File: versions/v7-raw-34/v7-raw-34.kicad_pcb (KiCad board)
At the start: 4 copper layers, 138.1 x 104.6 mm, 133 parts, among them J1 USB_C_Receptacle_USB2.0, J10 AXT-310124, J11 THD2528-11SD-GF, J12 SM04B-SRSS-TB_LF__SN_, J2 EXTENSION_HEADER, J3 USB_HDR, J4 Conn_01x08_Pin, J5 CONN_BAT, J6 FH34SRJ-6S-0.5SH_99_, J7 ESP_HDR, J8 ESP_XTR_HDR, J9 Conn_01x08_Pin, Q1 AO3401A, Q3 MMBT3904, Q4 MMBT3904, U1 RT9080-33GJ5, U10 ED060XC5, U11 TP4056, U12 RY3730, U2 PCA9535PW, U3 RSL48_4P4X4P4, U4 USBLC6-2P6, U5 XC6206PxxxMR, U6 RY3730, U8 ESP32-S3-WROOM-1, U9 CH340C

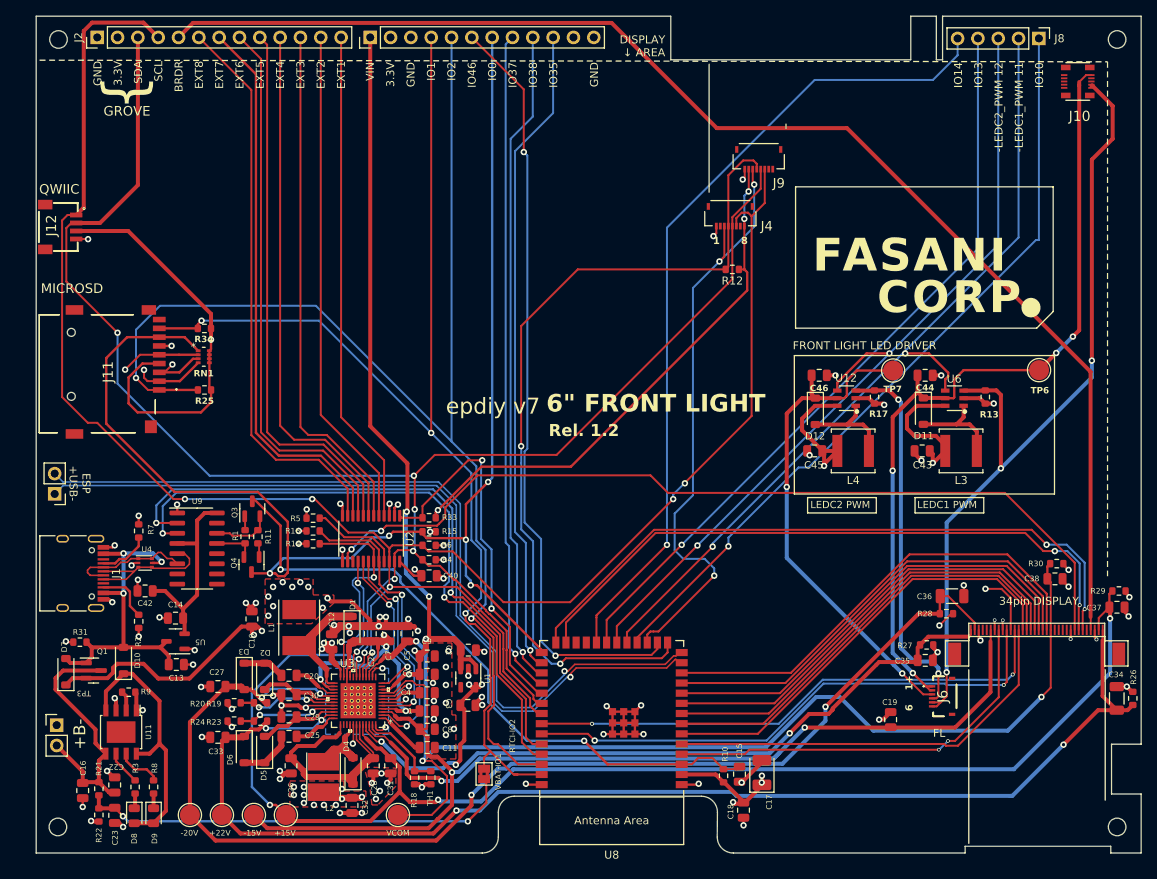
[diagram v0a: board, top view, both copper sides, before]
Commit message: Add kindle 34 pins versions (RAW)
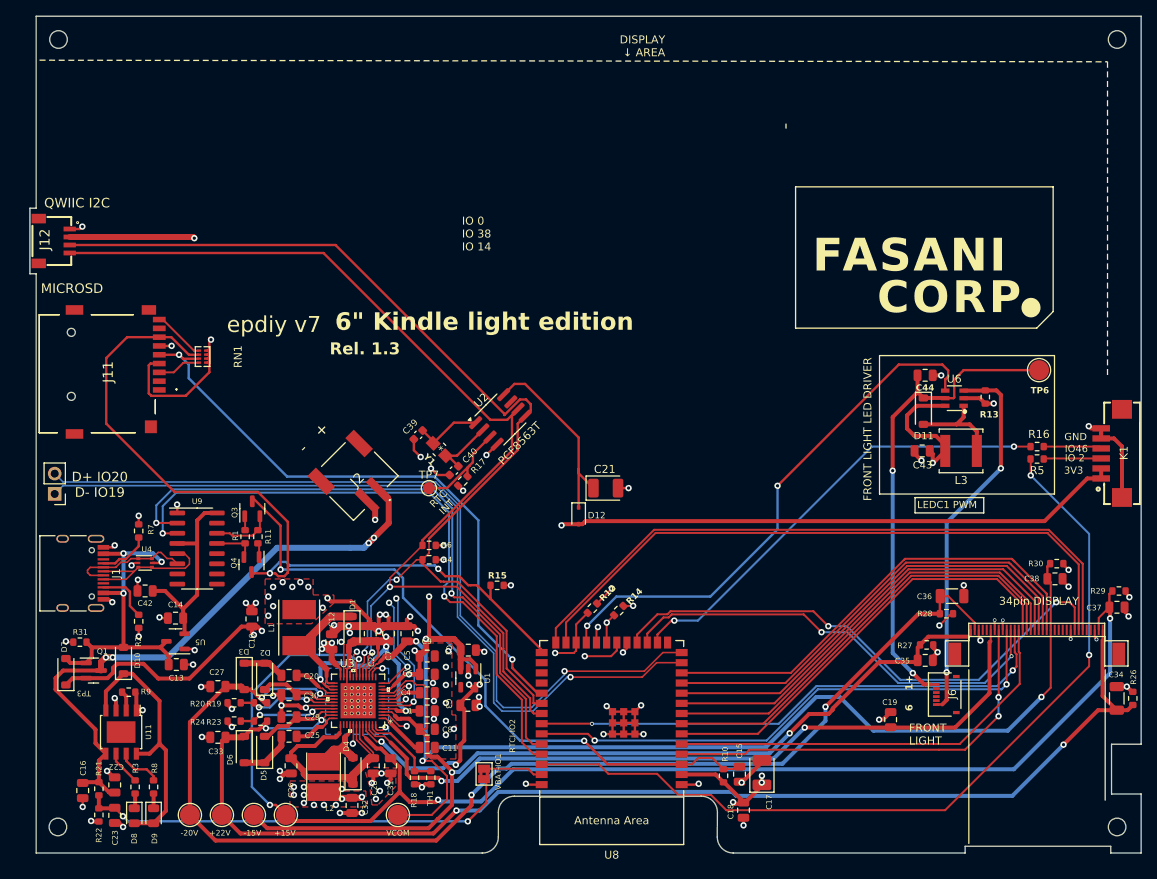
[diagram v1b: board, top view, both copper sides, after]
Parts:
- removed C45: 10uF, Capacitor_SMD:C_0805_2012Metric
- removed C46: 1uF/25V, Capacitor_SMD:C_0805_2012Metric
- removed J10: AXT-310124, footprint:AXT310124
- removed J4, J9: Conn_01x08_Pin, footprint:CONN8_FH34SRJ_HIR
- removed J5: CONN_BAT, Connector_PinHeader_2.54mm:PinHeader_1x02_P2.54mm_Vertical
- removed J7: ESP_HDR, Connector_PinHeader_2.54mm:PinHeader_1x12_P2.54mm_Vertical
- removed J8: ESP_XTR_HDR, Connector_PinHeader_2.54mm:PinHeader_1x05_P2.54mm_Vertical
- removed L4: L, footprint:SWPA5040S282MT
- removed R25, R34: 33k, Resistor_SMD:R_0603_1608Metric
- removed R33: 10k, Resistor_SMD:R_0603_1608Metric
- removed REF**: OSHW-Logo2_9.8x8mm_SilkScreen, Symbol:OSHW-Logo2_9.8x8mm_SilkScreen
- removed U12: RY3730, footprint:SOT-23-6_RY3730_Led_PWM
- added C21: C_Polarized 100uF, Capacitor_Tantalum_SMD:CP_EIA-3528-21_Kemet-B, F.Cu at (131.1, 103.0)
- added C39: 12 pF, Capacitor_SMD:C_0603_1608Metric, F.Cu at (107.6, 96.3)
- added K1: HC-1.25-6PWT, footprint:CONN-SMD_6P-P1.25_HC-1.25-6PWT, F.Cu at (194.3, 98.7)
- added Y1: Crystal_Small, footprint:Q13FC1350000400-Crystal, F.Cu at (110.3, 98.2)
- C40: value 100nF -> 12 pF; footprint Capacitor_SMD:C_0805_2012Metric -> Capacitor_SMD:C_0603_1608Metric
- D12: value MBR0540 -> 1N4148WS; footprint Diode_SMD:D_SOD-123 -> Diode_SMD:D_SOD-323
- J2: value EXTENSION_HEADER -> S2B-PH-SM4-TB_LF__SN_; footprint Connector_PinHeader_2.54mm:PinHeader_1x13_P2.54mm_Vertical -> footprint:S2BPHSM4TBLFSN
- J6: footprint footprint:FH34SRJ6S05SH99_Mirrored -> footprint:C224194_6x1_FH34SRJ-6S-0.5SH50_HIR
- L3: value L -> 22 uH
- R16: value 10k -> 0R
- R17: value 25Ω -> 10 K
- R3, R8: value 1k -> 2.4k
- R5: value 0 -> 0R
- R9: value 6.8k -> 3.8k
- RN1: footprint footprint:RESN_F392JTCE_UNR_SD-pullup -> footprint:C425297_RES-ARRAY-SMD_0402-8P-L2.0-W1.0-BL
- TP7: value C2 -> RTC_INT; footprint TestPoint:TestPoint_Pad_D2.5mm -> TestPoint:TestPoint_Pad_D1.5mm
- U2: value PCA9535PW -> PCF8563T; footprint Package_SO:TSSOP-24_4.4x7.8mm_P0.65mm -> Package_SO:SOIC-8_3.9x4.9mm_P1.27mm
- U3: value RSL48_4P4X4P4 -> TPS651851RSLR
- moved R16 91.1 mm to (185.0, 97.8), turned to 180 degrees
- moved R5 90.8 mm to (185.0, 99.3)
- moved J2 63.6 mm to (99.7, 101.5), turned to 45 degrees
- moved TP7 59.9 mm to (109.0, 103.0)
- moved R17 52.5 mm to (113.2, 102.1), turned to 45 degrees
- moved R12 45.8 mm to (129.4, 118.0), turned to -135 degrees
- moved R14 39.1 mm to (132.7, 118.3), turned to -135 degrees
- moved D12 32.3 mm to (127.7, 106.4)
- moved U2 22.0 mm to (117.9, 94.4), turned to 45 degrees
- moved C40 13.5 mm to (112.1, 100.8), turned to 45 degrees
- moved R15 10.8 mm to (117.5, 115.1)
- moved J12 1.93 mm to (59.4, 69.1)
- moved J6 0.23 mm to (173.4, 128.8)
- moved RN1 0.15 mm to (80.7, 86.5), turned to -90 degrees
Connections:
- C16 pad 2: BAT+ -> VBAT
- C22 pad 2: BAT+ -> VBAT
- C40 pad 1: 3.3V -> GND
- C40 pad 2: GND -> Net-(U2-OSCO)
- D12 pad 1: /LEDC2_A -> Net-(D12-K)
- D12 pad 2: Net-(D12-A) -> 3.3V
- J11 pad 1: /GPIO_2 -> unconnected-(J11-DAT2-Pad1)
- J11 pad 2: /GPIO_13 -> unconnected-(J11-CD/DAT3-Pad2)
- J11 pad 5: /GPIO_10 -> /GPIO_38
- J11 pad 8: /GPIO_1 -> unconnected-(J11-DAT1-Pad8)
- J11 pad 9: unconnected-(J11-CD-Pad9) -> /SD_CD
- J12 pad 1: /SCL -> GND
- J12 pad 2: /SDA -> 3.3V
- J12 pad 3: 3.3V -> /SDA
- J12 pad 4: GND -> /SCL
- J2 pad 1: GND -> VBAT
- J2 pad 2: 3.3V -> GND
- J6 pad 2: /LEDC1_A -> unconnected-(J6-Pad2)
- J6 pad 3: /LEDC2_A -> unconnected-(J6-Pad3)
- J6 pad 4: /LEDC2_KA -> unconnected-(J6-Pad4)
- J6 pad 5: /LEDC1_KA -> unconnected-(J6-Pad5)
- Q1 pad 3: BAT+ -> VBAT
- R12 pad 2: /TP_INT -> /TPS_PWR_GOOD
- R14 pad 2: /TPS_PWR_GOOD -> /TPS_nINT
- R16 pad 1: 3.3V -> Net-(K1-Pad4)
- R16 pad 2: /TPS_nINT -> RXD
- R17 pad 1: GND -> 3.3V
- R17 pad 2: /LEDC2_KA -> Net-(U2-~{INT})
- R21 pad 1: BAT+ -> VBAT
- R5 pad 1: Net-(U2-A0) -> Net-(K1-Pad3)
- R5 pad 2: GND -> TXD
- RN1 pad 1: /IO0 -> 3.3V
- RN1 pad 2: /GPIO_10 -> 3.3V
- RN1 pad 3: /GPIO_14 -> 3.3V
- RN1 pad 4: /GPIO_13 -> 3.3V
- RN1 pad 5: 3.3V -> /GPIO_14
- RN1 pad 6: 3.3V -> /GPIO_38
- RN1 pad 7: 3.3V -> /IO0
- RN1 pad 8: 3.3V -> /SD_CD
- TP7 pad 1: /LEDC2_A -> Net-(U2-~{INT})
- U11 pad 5: BAT+ -> VBAT
- U2 pad 1: /~{GPIO_INTR} -> Net-(U2-OSCI)
- U2 pad 2: GND -> Net-(U2-OSCO)
- U2 pad 3: GND -> Net-(U2-~{INT})
- U2 pad 4: /EXT1 -> GND
- U2 pad 5: /EXT2 -> /SDA
- U2 pad 6: /EXT3 -> /SCL
- U2 pad 7: /EXT4 -> unconnected-(U2-CLKO-Pad7)
- U2 pad 8: /EXT5 -> Net-(D12-K)
- U8 pad 16: /GPIO_46 -> RXD
- U8 pad 17: /TP_RST -> /EP_OE
- U8 pad 18: /GPIO_10 -> /EP_MODE
- U8 pad 19: /LEDC1_PWM -> /TPS_PWRUP
- U8 pad 20: /LEDC2_PWM -> /TPS_VCOM_CTRL
- U8 pad 21: /GPIO_13 -> /TPS_nINT
- U8 pad 22: /GPIO_14 -> /TPS_WAKEUP
- U8 pad 23: unconnected-(U8-GPIO21-Pad23) -> /LEDC1_PWM
- U8 pad 24: unconnected-(U8-GPIO47/SPICLK_P/SUBSPICLK_P_DIFF-Pad24) -> /TPS_PWR_GOOD
- U8 pad 31: /~{GPIO_INTR} -> /GPIO_38
- U8 pad 38: /GPIO_2 -> TXD
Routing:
- net /GPIO_10: track 200.6 -> 0.00 mm, vias 2 -> 0
- net /GPIO_13: track 188.0 -> 0.00 mm, vias 2 -> 0
- net /GPIO_14: track 188.6 -> 5.36 mm, vias 2 -> 0
- net /BORDER: track 165.1 -> 0.00 mm
- net /GPIO_2: track 161.9 -> 0.00 mm, vias 2 -> 0
- net /GPIO_1: track 146.0 -> 7.50 mm, vias 3 -> 0
- net /SCL: track 246.6 -> 136.1 mm, vias 6 -> 2
- net 3.3V: track 305.5 -> 195.6 mm, vias 17 -> 16
- net TXD: track 0.00 -> 107.2 mm, vias 0 -> 2
- net /TP_INT: track 105.7 -> 0.00 mm, vias 2 -> 0
- net /LEDC2_PWM: track 104.3 -> 0.00 mm, vias 2 -> 0
- net /GPIO_46: track 95.8 -> 0.00 mm, vias 2 -> 0
- net VIN: track 275.3 -> 183.8 mm, vias 23 -> 21
- net /GPIO_37: track 83.2 -> 0.00 mm, vias 1 -> 0
- net /GPIO_36: track 82.5 -> 0.00 mm, vias 1 -> 0
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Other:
- board size 138.1 x 104.6 mm -> 138.9 x 104.6 mm
- board text added: "+"
- board text added: "-"
- board text added: "3V3"
- board text added: "6{dblquote} Kindle light edition"
- board text added: "D+ IO20 D- IO19"
- board text added: "FRONT LIGHT"
- board text added: "IO 0 IO 38 IO 14"
- board text added: "IO 2"
- board text added: "PCF8563T"
- board text added: "QWIIC I2C"
- board text added: "RTC INT"
- board text added: "Rel. 1.3"
- board text removed: "+B-"
- board text removed: "-LEDC1_PWM 11"
- board text removed: "-LEDC2_PWM 12"
- board text removed: "1"
- board text removed: "3.3V"
- board text removed: "6{dblquote} FRONT LIGHT"
- board text removed: "8"
- board text removed: "BRDR"
- board text removed: "ESP +USB-"
- board text removed: "EXT1"
- board text removed: "EXT2"
- board text removed: "EXT3"
- board text removed: "EXT4"
- board text removed: "EXT5"
- board text removed: "EXT6"
- board text removed: "EXT7"
- board text removed: "EXT8"
- board text removed: "FL"
- board text removed: "GROVE"
- board text removed: "IO0"
- board text removed: "IO1"
- board text removed: "IO10"
- board text removed: "IO13"
- board text removed: "IO14"
- board text removed: "IO2"
- board text removed: "IO35"
- board text removed: "IO37"
- board text removed: "IO38"
- board text removed: "LEDC2 PWM"
- board text removed: "QWIIC"
- board text removed: "Rel. 1.2"
- board text removed: "SCL"
- board text removed: "SDA"
- board text removed: "VIN"
- board text removed: "{"
